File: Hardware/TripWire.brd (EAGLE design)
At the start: 32.3 x 50.2 mm, 50 parts, among them P1 LSP11, P2 LSP11, P3 LSP11, P4 LSP11, P5 LSP11, P6 LSP11, P7 LSP11, X1 GADGETEER-SOCKET

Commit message: Changed the OSHW logo to use the SparkFun medium one.
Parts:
- LOGO1: value LOGO-OSHW-FILLX0200-NT -> OSHW-LOGOM; device Logo:OSHW_FILLX200_NOTEXT -> SparkFun-Aesthetics:OSHW-LOGO-M
- moved LOGO1 29.6 mm to (23.3, 7.26)
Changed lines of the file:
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@@
 <layer number="14" name="Route14" color="1" fill="6" visible="no" active="no"/>
 <layer number="15" name="VCC" color="4" fill="6" visible="no" active="no"/>
-<layer number="16" name="Bottom" color="1" fill="1" visible="no" active="yes"/>
-<layer number="17" name="Pads" color="2" fill="1" visible="no" active="yes"/>
-<layer number="18" name="Vias" color="2" fill="1" visible="no" active="yes"/>
-<layer number="19" name="Unrouted" color="5" fill="1" visible="no" active="yes"/>
+<layer number="16" name="Bottom" color="1" fill="1" visible="yes" active="yes"/>
+<layer number="17" name="Pads" color="2" fill="1" visible="yes" active="yes"/>
+<layer number="18" name="Vias" color="2" fill="1" visible="yes" active="yes"/>
+<layer number="19" name="Unrouted" color="5" fill="1" visible="yes" active="yes"/>
 <layer number="20" name="Dimension" color="3" fill="1" visible="yes" active="yes"/>
 <layer number="21" name="tPlace" color="7" fill="1" visible="yes" active="yes"/>
 <layer number="22" name="bPlace" color="7" fill="1" visible="no" active="yes"/>
-<layer number="23" name="tOrigins" color="15" fill="1" visible="no" active="yes"/>
-<layer number="24" name="bOrigins" color="15" fill="1" visible="no" active="yes"/>
+<layer number="23" name="tOrigins" color="15" fill="1" visible="yes" active="yes"/>
+<layer number="24" name="bOrigins" color="15" fill="1" visible="yes" active="yes"/>
 <layer number="25" name="tNames" color="7" fill="1" visible="yes" active="yes"/>
 <layer number="26" name="bNames" color="7" fill="1" visible="no" active="yes"/>
-<layer number="27" name="tValues" color="7" fill="1" visible="yes" active="yes"/>
+<layer number="27" name="tValues" color="7" fill="1" visible="no" active="yes"/>
 <layer number="28" name="bValues" color="7" fill="1" visible="no" active="yes"/>
 <layer number="29" name="tStop" color="7" fill="3" visible="no" active="yes"/>
@@
 <attribute name="VALUE" x="13.5128" y="31.8262" size="0.8128" layer="27" ratio="12" rot="R180"/>
 </element>
-<element name="LOGO1" library="Logo" package="OSHW_FILLX200_NOTEXT" value="LOGO-OSHW-FILLX0200-NT" x="13.796" y="35.3428" rot="R270"/>
 <element name="U$1" library="SoftDust" package="SPADE-TERMINAL" value="SPADE-TERMINALPTH" x="27.7622" y="37.9222" smashed="yes" rot="R270"/>
 <element name="U$2" library="SoftDust" package="SPADE-TERMINAL" value="SPADE-TERMINALPTH" x="27.7622" y="32.8422" smashed="yes" rot="R270"/>
@@
 </element>
 <element name="VESD05A8A-HNH-GS08" library="SoftDust" package="8-UFDFN" value="VESD05A8A-HNH-GS088-UFDFN_TVS-DIODE-ARRAY" x="19.9644" y="33.02" smashed="yes"/>
+<element name="LOGO1" library="SparkFun-Aesthetics" package="OSHW-LOGO-M" value="OSHW-LOGOM" x="23.2664" y="7.2644" rot="R270"/>
 </elements>
 <signals>

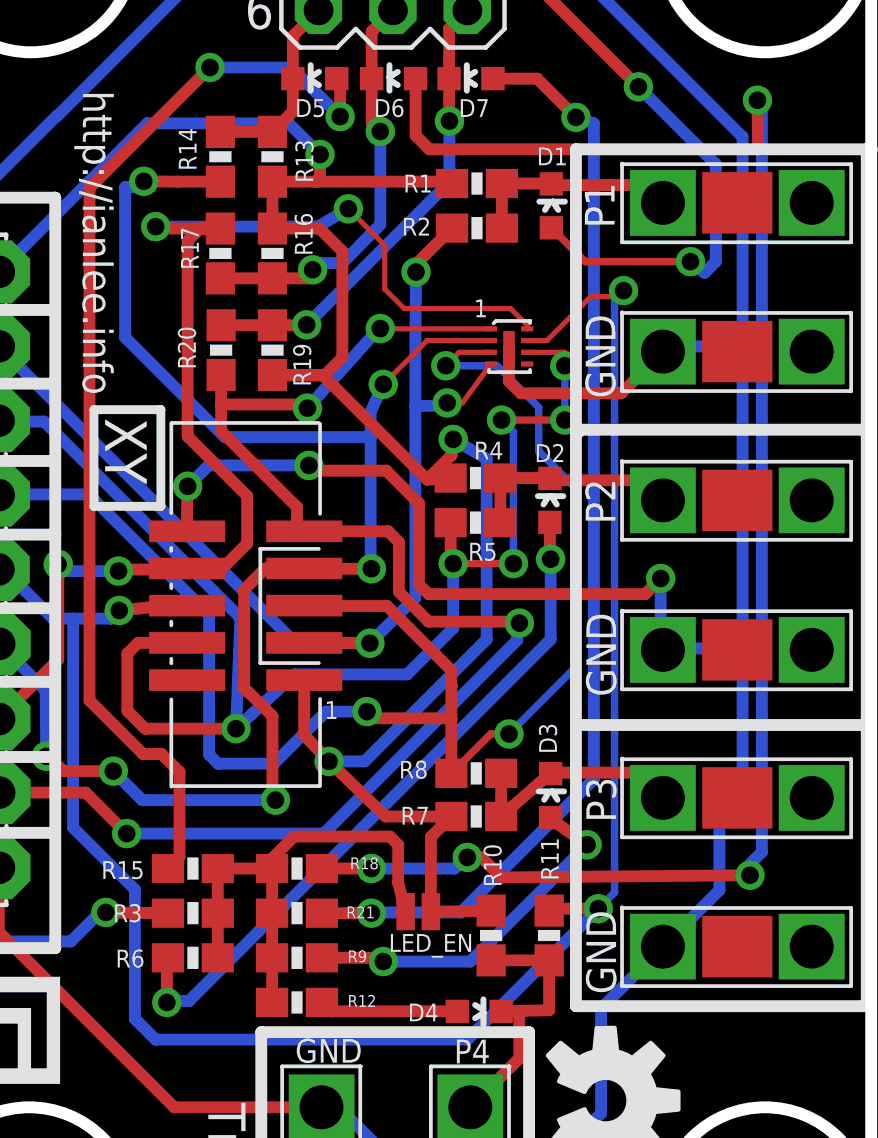
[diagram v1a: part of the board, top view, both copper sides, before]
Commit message: Merged 3V3 & 3V3_B nets.
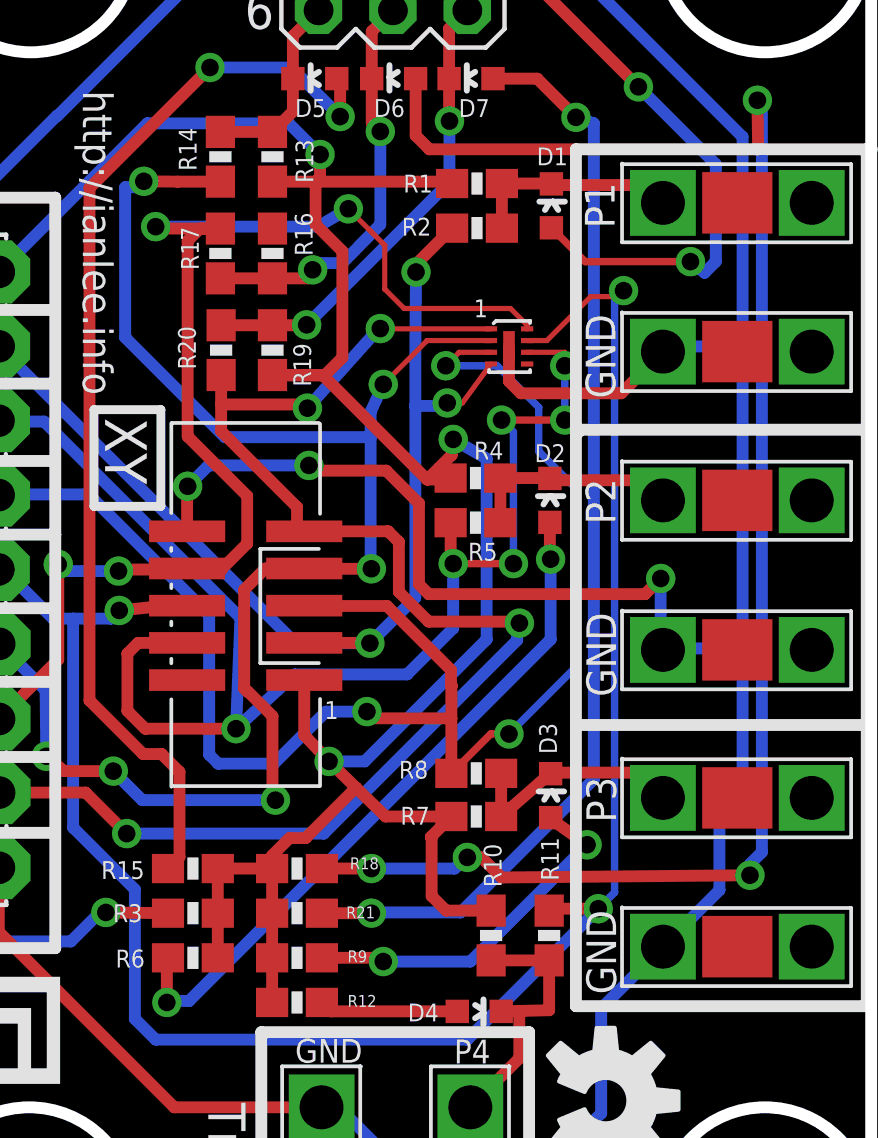
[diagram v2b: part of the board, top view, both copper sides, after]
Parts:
- removed LED_EN: SOLDER-JUNCTION, SoftDust:SOLDER-JUNCTION
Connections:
- removed net 3V3_B: LED_EN.2, R12.1, R15.1, R18.2, R21.1, R3.1, R6.2, R9.1
- net 3V3: now also R12.1, R15.1, R18.2, R21.1, R3.1, R6.2, R9.1; no longer LED_EN.1, R16.1
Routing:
- net 3V3_B: track 16.9 -> 0.00 mm
- net 3V3: track 68.8 -> 80.7 mm
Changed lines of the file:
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@@
 <layer number="20" name="Dimension" color="3" fill="1" visible="yes" active="yes"/>
 <layer number="21" name="tPlace" color="7" fill="1" visible="yes" active="yes"/>
-<layer number="22" name="bPlace" color="7" fill="1" visible="no" active="yes"/>
+<layer number="22" name="bPlace" color="7" fill="1" visible="yes" active="yes"/>
 <layer number="23" name="tOrigins" color="15" fill="1" visible="yes" active="yes"/>
 <layer number="24" name="bOrigins" color="15" fill="1" visible="yes" active="yes"/>
@@
 <attribute name="VALUE" x="11.5824" y="13.462" size="0.4064" layer="27" font="vector"/>
 </element>
-<element name="LED_EN" library="SoftDust" package="SOLDER-JUNCTION" value="SOLDER-JUNCTION" x="16.8656" y="13.716" smashed="yes" rot="R180">
-<attribute name="NAME" x="18.7452" y="12.954" size="0.6096" layer="25" rot="R180"/>
-</element>
 <element name="P2" library="solpad" package="LSP11" value="LSP11" x="2.5286" y="30.4838" smashed="yes" rot="R90">
 <attribute name="NAME" x="0.3416" y="31.3906" size="1.016" layer="25" ratio="10" rot="SR270"/>
@@
 <contactref element="X1" pad="1"/>
 <contactref element="R13" pad="1"/>
-<contactref element="R16" pad="1"/>
 <contactref element="R19" pad="1"/>
 <contactref element="R1" pad="1"/>
@@
 <contactref element="R7" pad="1"/>
 <contactref element="R10" pad="1"/>
-<wire x1="11.8872" y1="37.045" x2="11.8872" y2="38.647" width="0.4064" layer="1"/>
-<contactref element="LED_EN" pad="1"/>
 <wire x1="19.3548" y1="13.7532" x2="19.343" y2="13.7414" width="0.4064" layer="1"/>
-<wire x1="19.343" y1="13.7414" x2="17.2974" y2="13.716" width="0.4064" layer="1"/>
 <wire x1="11.8872" y1="38.647" x2="13.3604" y2="38.647" width="0.4064" layer="1"/>
 <wire x1="13.3604" y1="38.647" x2="17.9578" y2="38.647" width="0.4064" layer="1"/>
 <wire x1="17.9578" y1="38.647" x2="18.0222" y2="38.5826" width="0.4064" layer="1"/>
-<wire x1="11.8872" y1="37.045" x2="13.501" y2="37.045" width="0.4064" layer="1"/>
-<wire x1="13.501" y1="37.045" x2="14.2748" y2="36.2712" width="0.4064" layer="1"/>
+<wire x1="13.3604" y1="37.1856" x2="14.2748" y2="36.2712" width="0.4064" layer="1"/>
 <wire x1="14.2748" y1="36.2712" x2="14.2748" y2="32.639" width="0.4064" layer="1"/>
 <wire x1="14.2748" y1="32.639" x2="13.6652" y2="32.0294" width="0.4064" layer="1"/>
@@
 <wire x1="17.1704" y1="28.4734" x2="17.9206" y2="28.4734" width="0.4064" layer="1"/>
 <wire x1="17.9206" y1="28.4734" x2="17.9714" y2="28.5242" width="0.4064" layer="1"/>
-<wire x1="17.2974" y1="13.716" x2="17.2974" y2="16.2678" width="0.4064" layer="1"/>
 <wire x1="17.2974" y1="16.2678" x2="17.9968" y2="16.9672" width="0.4064" layer="1"/>
 <wire x1="17.1704" y1="28.4734" x2="18.0086" y2="29.3116" width="0.4064" layer="1"/>
@@
 <via x="13.8197" y="18.8489" extent="1-16" drill="0.6" shape="square"/>
 <wire x1="17.9968" y1="16.9672" x2="15.7522" y2="16.9672" width="0.4064" layer="1"/>
-<wire x1="15.7522" y1="16.9672" x2="13.8197" y2="18.8489" width="0.4064" layer="1"/>
+<wire x1="15.7522" y1="16.9672" x2="14.7412875" y2="17.9515375" width="0.4064" layer="1"/>
+<wire x1="14.7412875" y1="17.9515375" x2="13.8197" y2="18.8489" width="0.4064" layer="1"/>
 <wire x1="7.615" y1="40.64" x2="12.446" y2="40.64" width="0.4064" layer="16"/>
 <wire x1="12.446" y1="40.64" x2="13.5128" y2="39.5732" width="0.4064" layer="16"/>
@@
 <contactref element="3V3" pad="MP"/>
 <wire x1="7.615" y1="40.64" x2="2.5388" y2="35.5638" width="0.4064" layer="16"/>
+<contactref element="R15" pad="1"/>
+<contactref element="R18" pad="2"/>
+<contactref element="R21" pad="1"/>
+<contactref element="R3" pad="1"/>
+<contactref element="R6" pad="2"/>
+<contactref element="R9" pad="1"/>
+<contactref element="R12" pad="1"/>
+<wire x1="11.8754" y1="10.6172" x2="11.8754" y2="12.1412" width="0.4064" layer="1"/>
+<wire x1="11.8754" y1="12.1412" x2="11.8754" y2="13.6652" width="0.4064" layer="1"/>
+<wire x1="11.8754" y1="13.6652" x2="11.8754" y2="15.1892" width="0.4064" layer="1"/>
+<wire x1="10.0194" y1="13.6652" x2="10.0194" y2="12.1412" width="0.4064" layer="1"/>
+<wire x1="10.0194" y1="13.6652" x2="10.0194" y2="15.1892" width="0.4064" layer="1"/>
+<wire x1="19.3548" y1="13.7532" x2="17.819" y2="13.7532" width="0.4064" layer="1"/>
+<wire x1="17.819" y1="13.7532" x2="17.3228" y2="14.2494" width="0.4064" layer="1"/>
+<wire x1="17.3228" y1="14.2494" x2="17.3228" y2="16.2424" width="0.4064" layer="1"/>
+<wire x1="17.3228" y1="16.2424" x2="17.2974" y2="16.2678" width="0.4064" layer="1"/>
+<wire x1="10.0194" y1="15.1892" x2="11.8754" y2="15.1892" width="0.4064" layer="1"/>
+<wire x1="11.8754" y1="15.1892" x2="11.8754" y2="15.6346" width="0.4064" layer="1"/>
+<wire x1="11.8754" y1="15.6346" x2="12.4714" y2="16.2306" width="0.4064" layer="1"/>
+<wire x1="12.4714" y1="16.2306" x2="13.02035" y2="16.2306" width="0.4064" layer="1"/>
+<wire x1="13.02035" y1="16.2306" x2="14.7412875" y2="17.9515375" width="0.4064" layer="1"/>
+<wire x1="13.3604" y1="38.647" x2="13.3604" y2="37.1856" width="0.4064" layer="1"/>
 </signal>
 <signal name="GND" class="1">
@@
 <wire x1="16.002" y1="47.037" x2="13.462" y2="47.037" width="0.4064" layer="16"/>
 <wire x1="25.146" y1="25.0952" x2="25.2222" y2="25.019" width="0.4064" layer="16"/>
-<wire x1="25.146" y1="22.733" x2="25.146" y2="22.86" width="0.4064" layer="16"/>
-<wire x1="25.146" y1="22.86" x2="25.146" y2="25.0952" width="0.4064" layer="16"/>
+<wire x1="25.146" y1="22.6568" x2="25.146" y2="25.0952" width="0.4064" layer="16"/>
 <wire x1="25.2222" y1="22.6568" x2="25.273" y2="22.7076" width="0.4064" layer="16"/>
 <wire x1="25.273" y1="22.7076" x2="27.94" y2="22.7076" width="0.4064" layer="16"/>
@@
 <wire x1="20.3708" y1="31.4198" x2="23.7998" y2="31.4198" width="0.4064" layer="1"/>
 <wire x1="25.2222" y1="22.6568" x2="25.146" y2="22.6568" width="0.4064" layer="16"/>
-<wire x1="25.146" y1="22.6568" x2="25.146" y2="22.733" width="0.4064" layer="16"/>
 <wire x1="25.2476" y1="32.8676" x2="25.2222" y2="32.8422" width="0" layer="19" extent="16-16"/>
 </signal>
@@
 <wire x1="5.6388" y1="20.9296" x2="5.6388" y2="38.4302" width="0.4064" layer="1"/>
 </signal>
-<signal name="3V3_B">
-<contactref element="R15" pad="1"/>
-<contactref element="R18" pad="2"/>
-<contactref element="R21" pad="1"/>
-<contactref element="R3" pad="1"/>
-<contactref element="R6" pad="2"/>
-<contactref element="R9" pad="1"/>
-<contactref element="R12" pad="1"/>
-<contactref element="LED_EN" pad="2"/>
-<wire x1="11.8754" y1="10.6172" x2="11.8754" y2="12.1412" width="0.4064" layer="1"/>
-<wire x1="11.8754" y1="12.1412" x2="11.8754" y2="13.6652" width="0.4064" layer="1"/>
-<wire x1="11.8754" y1="13.6652" x2="11.8754" y2="15.1892" width="0.4064" layer="1"/>
-<wire x1="10.0194" y1="15.1892" x2="11.8754" y2="15.1892" width="0.4064" layer="1"/>
-<wire x1="10.0194" y1="15.1892" x2="10.0194" y2="13.6652" width="0.4064" layer="1"/>
-<wire x1="10.0194" y1="13.6652" x2="10.0194" y2="12.1412" width="0.4064" layer="1"/>
-<wire x1="16.4338" y1="13.716" x2="16.1798" y2="14.7066" width="0.4064" layer="1"/>
-<wire x1="16.1798" y1="14.7066" x2="16.1798" y2="16.002" width="0.4064" layer="1"/>
-<wire x1="16.1798" y1="16.002" x2="15.9004" y2="16.2814" width="0.4064" layer="1"/>
-<wire x1="15.9004" y1="16.2814" x2="12.6238" y2="16.2814" width="0.4064" layer="1"/>
-<wire x1="12.6238" y1="16.2814" x2="11.8754" y2="15.533" width="0.4064" layer="1"/>
-<wire x1="11.8754" y1="15.533" x2="11.8754" y2="15.1892" width="0.4064" layer="1"/>
-</signal>
 <signal name="N$9">

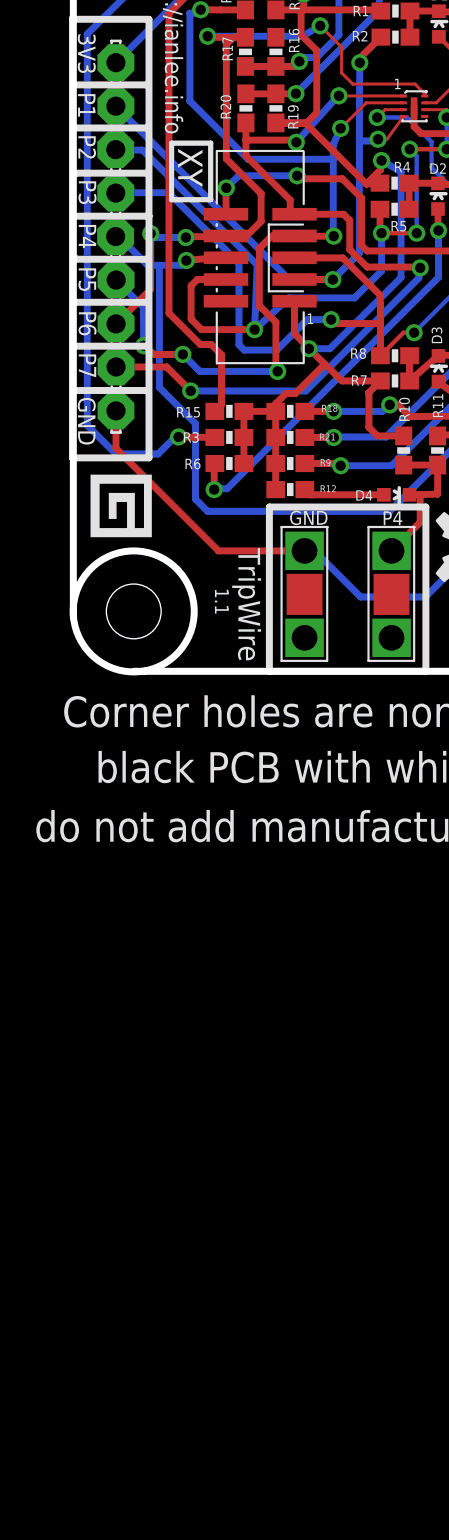
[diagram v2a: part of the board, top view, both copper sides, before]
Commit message: Added 100 Ohm resistors to IO pins.
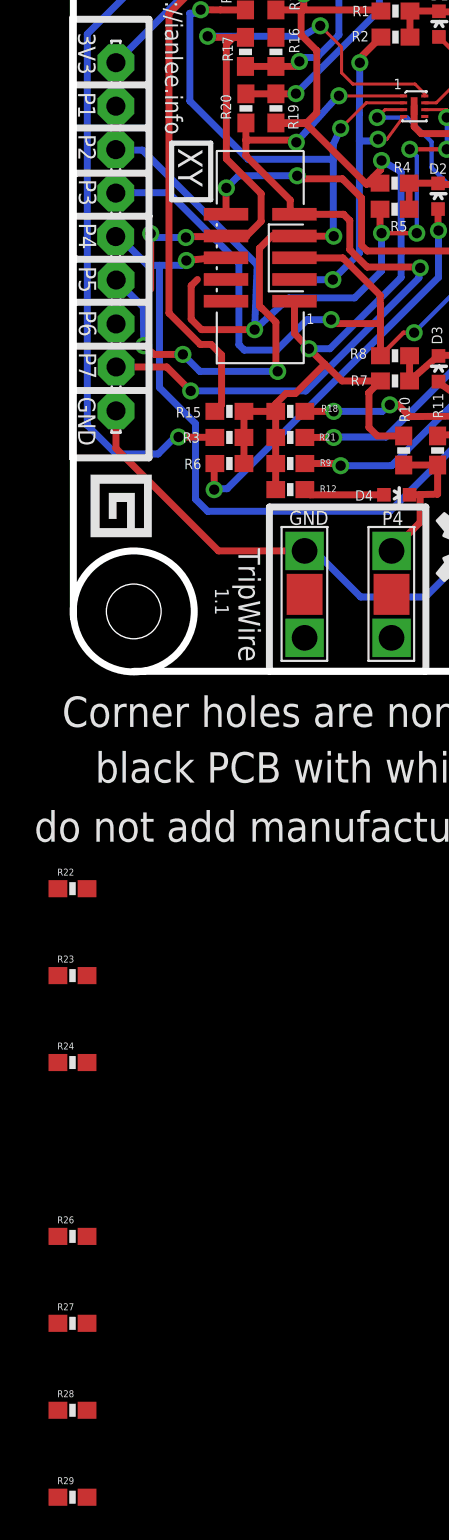
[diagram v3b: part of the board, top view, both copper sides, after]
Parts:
- added R22, R23, R24, R26, R27, R28, R29: 10, SparkFun-Resistors:0603-RES
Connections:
- new net N$15: P2.MP, R22.1, X1.4
- new net N$16: P4.MP, R23.1, X1.6
- new net N$17: P6.MP, R24.1, X1.8
- new net N$18: P1.MP, R26.2, X1.3
- new net N$19: P3.MP, R27.2, X1.5
- new net N$20: P5.MP, R28.2, X1.7
- new net N$21: P7.MP, R29.2, X1.9
- net PIN3: now also R26.1; no longer P1.MP, X1.3
- net PIN4: now also R22.2; no longer P2.MP, X1.4
- net PIN5: now also R27.1; no longer P3.MP, X1.5
- net PIN6: now also R23.2; no longer P4.MP, X1.6
- net PIN7: now also R28.1; no longer P5.MP, X1.7
- net PIN8: now also R24.2; no longer P6.MP, X1.8
- net PIN9: now also R29.1; no longer P7.MP, X1.9
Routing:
- net PIN9: track 48.3 -> 16.6 mm, vias 4 -> 2
- net N$21: track 0.00 -> 31.3 mm, vias 0 -> 2
- net PIN7: track 54.2 -> 31.2 mm, vias 6 -> 3
- net N$20: track 0.00 -> 22.9 mm, vias 0 -> 3
- net PIN3: track 37.8 -> 21.2 mm
- net PIN8: track 44.4 -> 41.5 mm
- net PIN4: track 48.3 -> 46.5 mm
